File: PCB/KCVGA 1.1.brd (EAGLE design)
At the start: 50 x 50 mm, 49 parts, among them IC1 M68AW128MND, IC2 74245ADB, IC3 74245ADB, IC4 LD117AS12TR, IC5 LD117AS33TR, U1 XC3S50ATQ144, U2 PIC32MX250F128B_I_SS, X1 D-SUB15, X2 MINI-USB

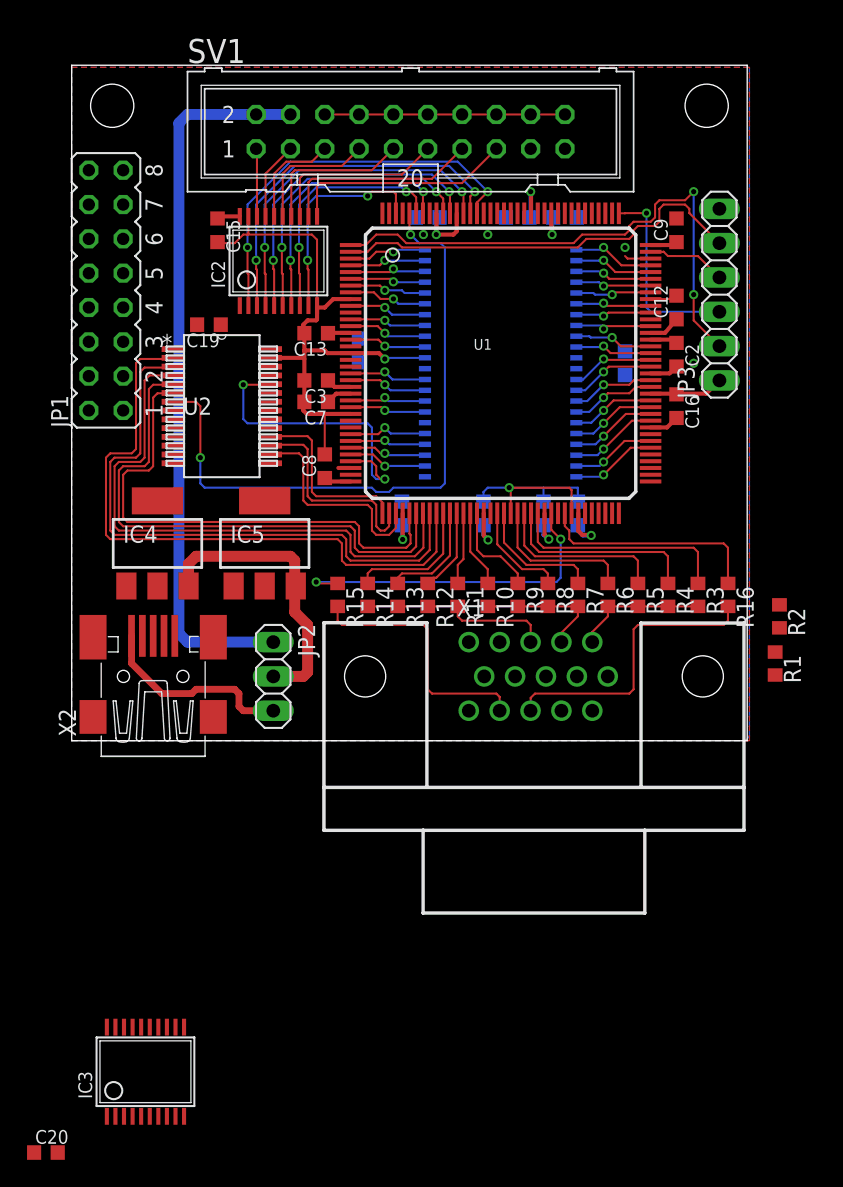
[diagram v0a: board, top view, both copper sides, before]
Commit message: Added crystal oscillator, voltage regulators, FPGA config lines
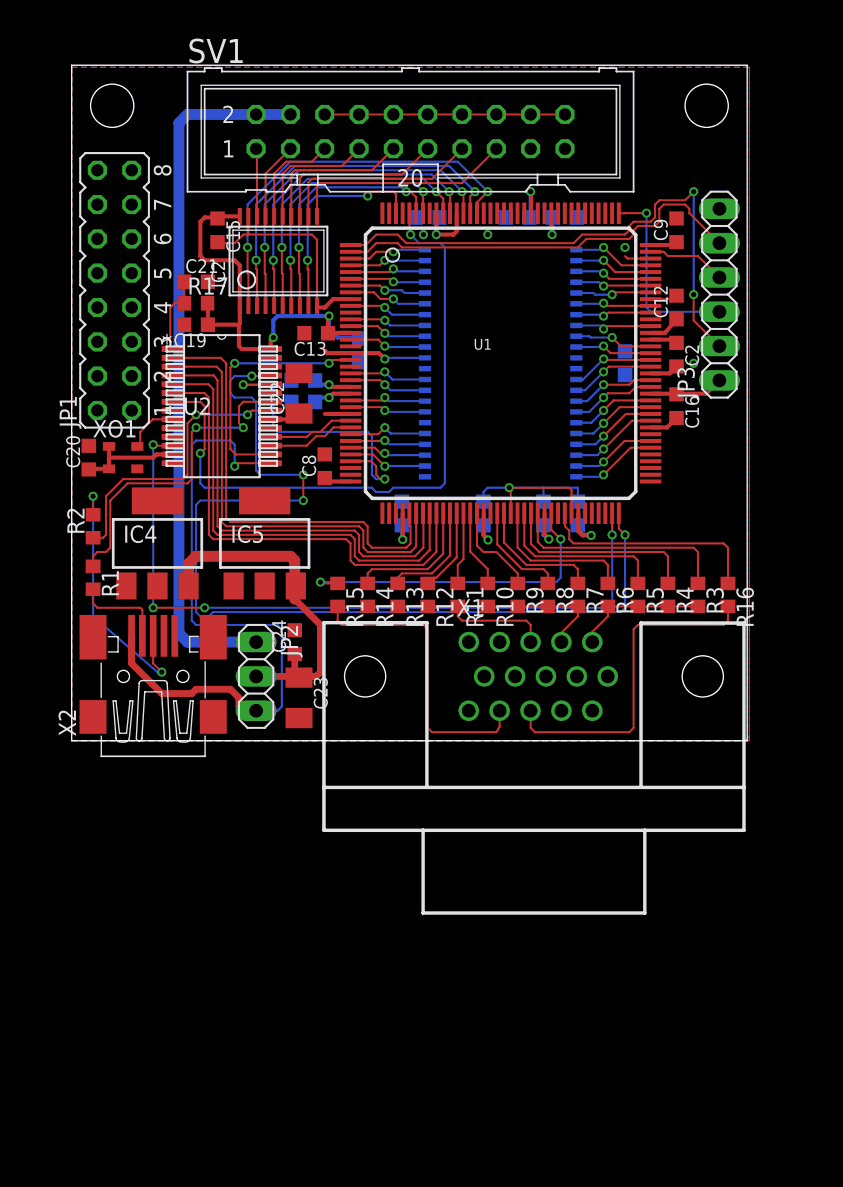
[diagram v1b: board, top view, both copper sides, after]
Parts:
- removed IC3: 74245ADB, 74xx-eu:SSOP20D8
- added C21, C24: 100n, rcl:C0603K
- added C22, C23: 10u, rcl:C1206K
- added R17: 10k, rcl:R0603
- added XO1: 32MHz, crystal:ASE
- moved C20 51.5 mm to (1.27, 21.0), turned to 90 degrees
- moved R2 51.2 mm to (1.59, 15.9), turned to 90 degrees
- moved R1 50.9 mm to (1.59, 12.1)
- moved JP2 1.27 mm to (13.7, 4.76)
- moved C19 0.95 mm to (9.21, 30.8)
- moved C3 0.95 mm to (17.1, 26.7), flipped to the bottom, turned to 0 degrees
- moved C7 0.95 mm to (17.1, 25.1), flipped to the bottom, turned to 0 degrees
- moved JP1 0.63 mm to (3.17, 33.3)
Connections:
- removed net VCAP: U2.20
- removed net VCC: IC3.20
- removed net VUSB3V3: U2.23
- new net CLK_32M: U2.9, XO1.3
- new net FPGA_CCLK: U1.P72, U2.25
- new net FPGA_CLK: U2.10
- new net FPGA_DIN: U1.P71, U2.12
- new net N$16: C22.1, U2.20
- new net NRESET: C21.1, R17.1, U2.1
- net +5V: now also C23.1, C24.1
- net 3V3: now also R17.2, U1.P143, U1.P37, U1.P38, U1.P39, U2.23, XO1.1, XO1.4
- net GND: now also C21.2, C22.2, C23.2, C24.2, XO1.2; no longer IC3.10
- net PMD1: now also U1.P44; no longer U1.P42
- net PMD2: now also U1.P45; no longer U1.P41
- net PMD3: now also U1.P27; no longer U1.P37
- net PMD4: now also U1.P28; no longer U1.P38
- net PMD5: now also U1.P18; no longer U1.P39
- net PMD6: now also U1.P42; no longer U1.P44
- net PMD7: now also U1.P41; no longer U1.P45
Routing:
- net FPGA_CCLK: track 0.00 -> 72.2 mm, vias 0 -> 4
- net FPGA_DIN: track 0.00 -> 54.3 mm, vias 0 -> 4
- net 3V3: track 36.4 -> 76.2 mm, vias 5 -> 8
- net N$1: track 14.8 -> 48.8 mm, vias 0 -> 1
- net N$11: track 0.00 -> 24.1 mm, vias 0 -> 2
- net N$12: track 0.00 -> 20.9 mm, vias 0 -> 2
- net N$14: track 0.00 -> 20.1 mm, vias 0 -> 2
- net GND: track 89.3 -> 71.1 mm
- net PMD7: track 46.8 -> 33.2 mm
- net PMD6: track 44.5 -> 33.6 mm
- net PMD4: track 15.5 -> 6.48 mm
- net PMD0: track 42.3 -> 34.0 mm
- net PMD3: track 13.4 -> 6.42 mm
- net N$13: track 0.00 -> 6.82 mm
- net NRESET: track 0.00 -> 5.94 mm
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
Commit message: completed FPGA configuration interface, tidied up
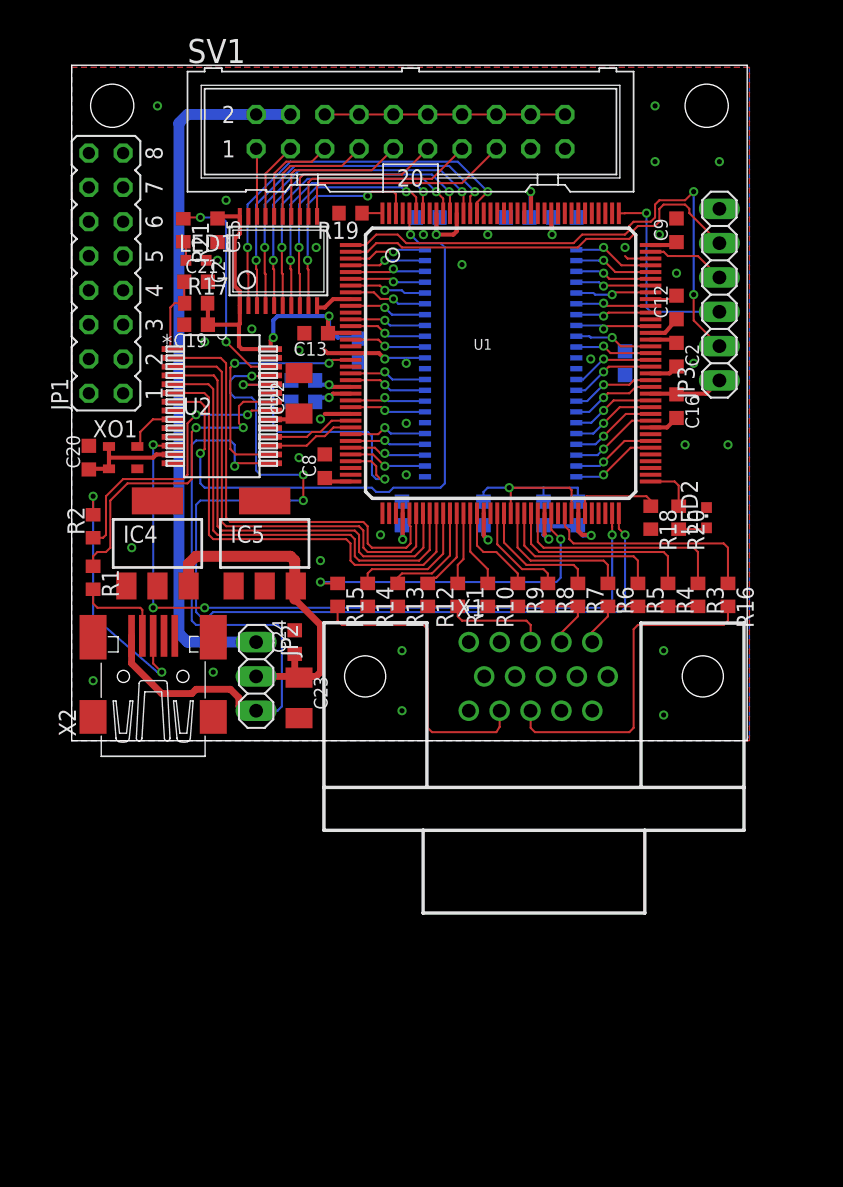
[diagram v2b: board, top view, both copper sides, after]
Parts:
- added LED1, LED2: (no value), led:CHIPLED_0603
- added R18, R19: 10k, rcl:R0603
- added R20, R21: 330, rcl:R0603
- moved JP1 1.42 mm to (2.54, 34.6)
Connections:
- net BHE renamed !BHE
- net BLE renamed !BLE
- net CE renamed !CE
- net NRESET renamed !RESET
- net OE renamed !OE
- net PMRD renamed !PMRD
- net PMWR renamed !PMWR
- net WE renamed !WE
- new net !INIT_B: R18.1, U1.P67, U2.14
- new net !PROG_B: R19.1, U1.P144, U2.11
- new net DONE: R20.1, U1.P73
- new net N$21: LED2.A, R20.2
- new net N$22: R21.1, U2.26
- new net N$23: LED1.A, R21.2
- net 3V3: now also R18.2, R19.2
- net GND: now also LED1.C, LED2.C, U1.P74
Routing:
- net N$22: track 0.00 -> 16.3 mm, vias 0 -> 2
- net GND: track 71.1 -> 57.2 mm, vias 6 -> 36
- net !INIT_B: track 0.00 -> 6.61 mm
- net DONE: track 0.00 -> 3.73 mm
- net N$21: track 0.00 -> 2.11 mm
- net !PROG_B: track 0.00 -> 1.52 mm
- net N$23: track 0.00 -> 1.46 mm
- net 3V3: track 76.2 -> 75.7 mm

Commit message: PCB: First implementation complete
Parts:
- JP1: device jumper:JP8Q -> pinhead:1X06
- moved C14 1.59 mm to (27.9, 38.7), turned to 180 degrees
- moved JP1 1.59 mm to (2.54, 33.0), turned to 270 degrees
- moved JP3 0.32 mm to (47.6, 33.0)
- moved C6 0.32 mm to (41.3, 27.9)
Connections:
- new net !FPGA_RESET: U1.P19
- net !RESET: now also JP1.1
- net 3V3: now also JP1.2
- net FPGA_CLK: now also U1.P127
- net GND: now also JP1.3
- net PMD0: now also JP1.4
- net PMD1: now also JP1.5
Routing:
- net 3V3: track 75.7 -> 237.7 mm, vias 8 -> 17
- net VCCINT: track 11.8 -> 83.1 mm, vias 3 -> 5
- net FPGA_CLK: track 0.00 -> 43.3 mm, vias 0 -> 2
- net !INIT_B: track 6.61 -> 48.2 mm, vias 0 -> 6
- net !PROG_B: track 1.52 -> 30.7 mm, vias 0 -> 2
- net !RESET: track 5.94 -> 16.8 mm
- net PMD0: track 34.0 -> 43.3 mm
- net PMD1: track 34.3 -> 41.8 mm
- net N$20: track 52.3 -> 57.6 mm
- net GND: track 57.2 -> 53.6 mm, vias 36 -> 49
- net N$1: track 48.8 -> 51.8 mm
- net +5V: track 26.8 -> 25.3 mm
- net D8: track 5.64 -> 6.98 mm
- net FPGA_CCLK: track 72.2 -> 73.4 mm
- net !PMWR: track 49.0 -> 50.1 mm
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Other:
- board text added: "1"

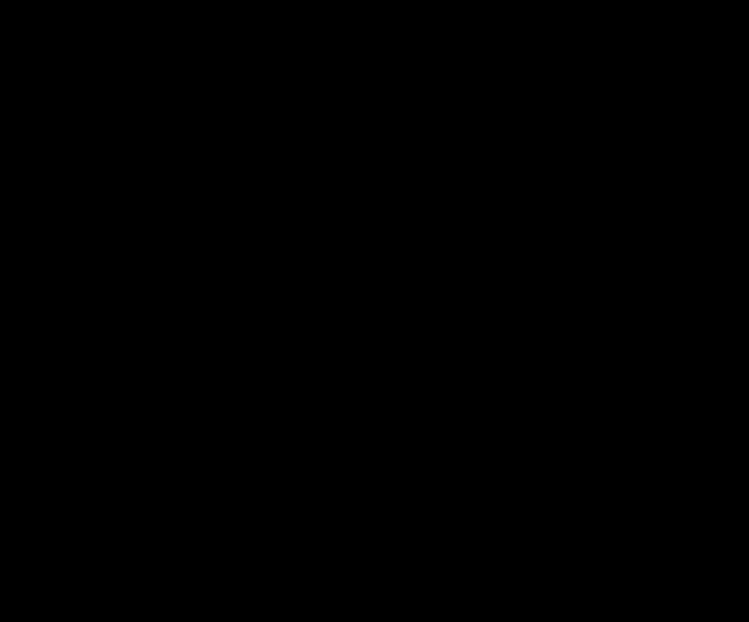
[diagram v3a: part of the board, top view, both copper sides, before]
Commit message: Test with PIC32MX270 in TQFP44
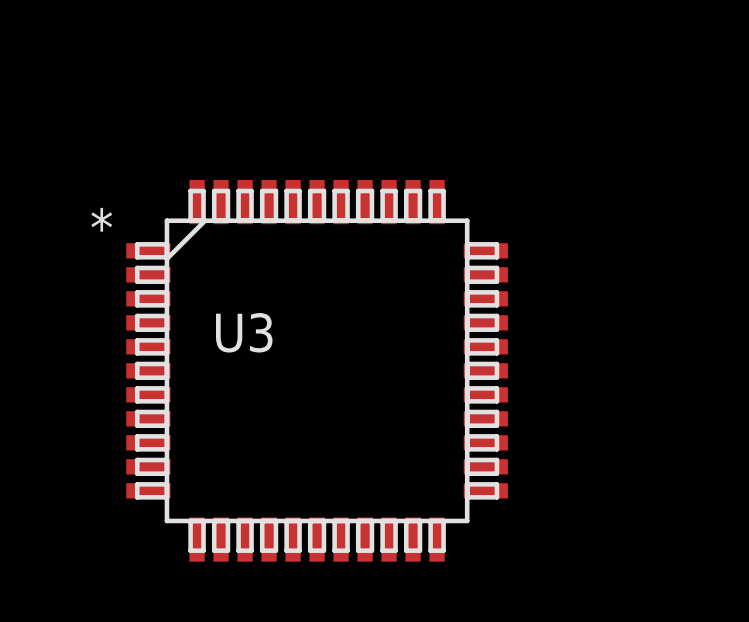
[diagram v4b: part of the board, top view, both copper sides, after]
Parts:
- added U3: PIC32MX270F256D, PIC32MX270:QFP44_10X10MC
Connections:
- new net AVDD: U3.17
- new net AVSS: U3.16
- new net VBUS: U3.42
- new net VCAP: U3.7
- new net VDD: U3.40
- new net VDD_2: U3.28
- new net VSS: U3.39
- new net VSS_2: U3.6
- new net VSS_3: U3.29
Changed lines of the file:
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@@
 <element name="R21" library="rcl" package="R0603" value="330" x="8.255" y="37.7825" rot="R270"/>
 <element name="JP1" library="pinhead" package="1X06" value="" x="2.54" y="33.02" rot="R270"/>
+<element name="U3" library="PIC32MX270" package="QFP44_10X10MC" value="PIC32MX270F256D" x="6.985" y="-20.0025"/>
 </elements>
 <signals>
@@
 <contactref element="U1" pad="P19"/>
 </signal>
+<signal name="VSS_2">
+<contactref element="U3" pad="6"/>
+</signal>
+<signal name="VCAP">
+<contactref element="U3" pad="7"/>
+</signal>
+<signal name="AVSS">
+<contactref element="U3" pad="16"/>
+</signal>
+<signal name="AVDD">
+<contactref element="U3" pad="17"/>
+</signal>
+<signal name="VDD_2">
+<contactref element="U3" pad="28"/>
+</signal>
+<signal name="VSS_3">
+<contactref element="U3" pad="29"/>
+</signal>
+<signal name="VSS">
+<contactref element="U3" pad="39"/>
+</signal>
+<signal name="VDD">
+<contactref element="U3" pad="40"/>
+</signal>
+<signal name="VBUS">
+<contactref element="U3" pad="42"/>
+</signal>
 </signals>
